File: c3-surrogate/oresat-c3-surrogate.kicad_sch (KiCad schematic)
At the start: 62 parts, among them J1 J-SAMTEC-TFM-120-X1-XXX-D-RA, J2 Conn_01x04, J3 Terminal Block, J4 Barrel Jack, J5 Header, J6 Header, Q1 PMV45EN, Q2 DMP3050LVT-7, Q3 PMV45EN, Q4 DMP3050LVT-7, SW1 Slide Switch, SW2 Slide Switch, U1 Trinket-M0, U2 Seeed-USB-to-UART, U3 MAX892LEUA+T

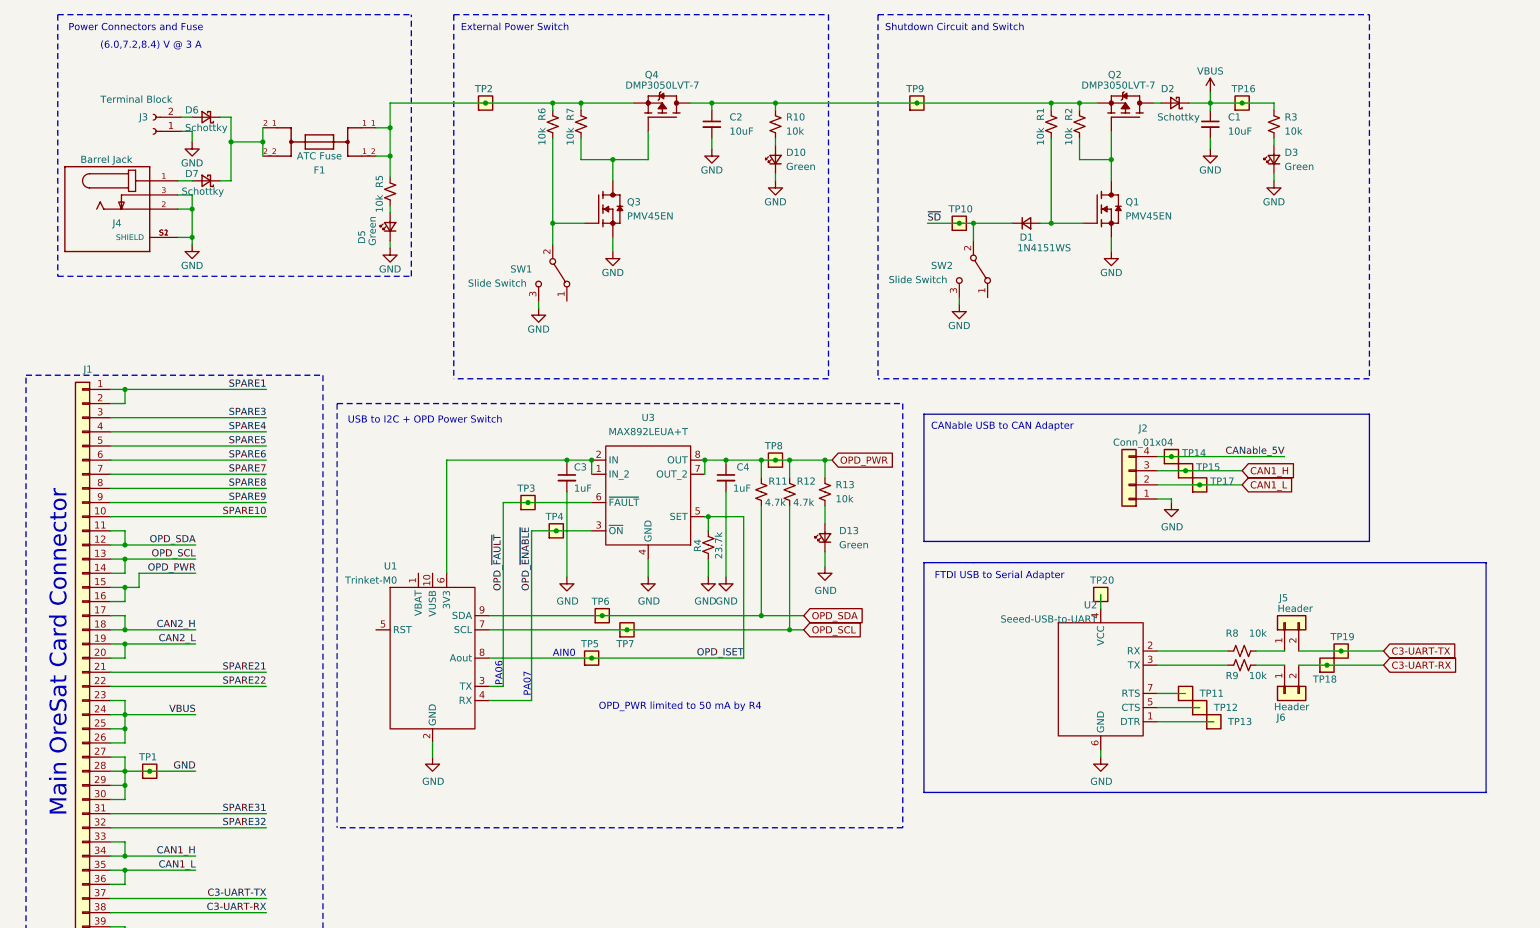
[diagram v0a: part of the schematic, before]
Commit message: updated c3 schematic
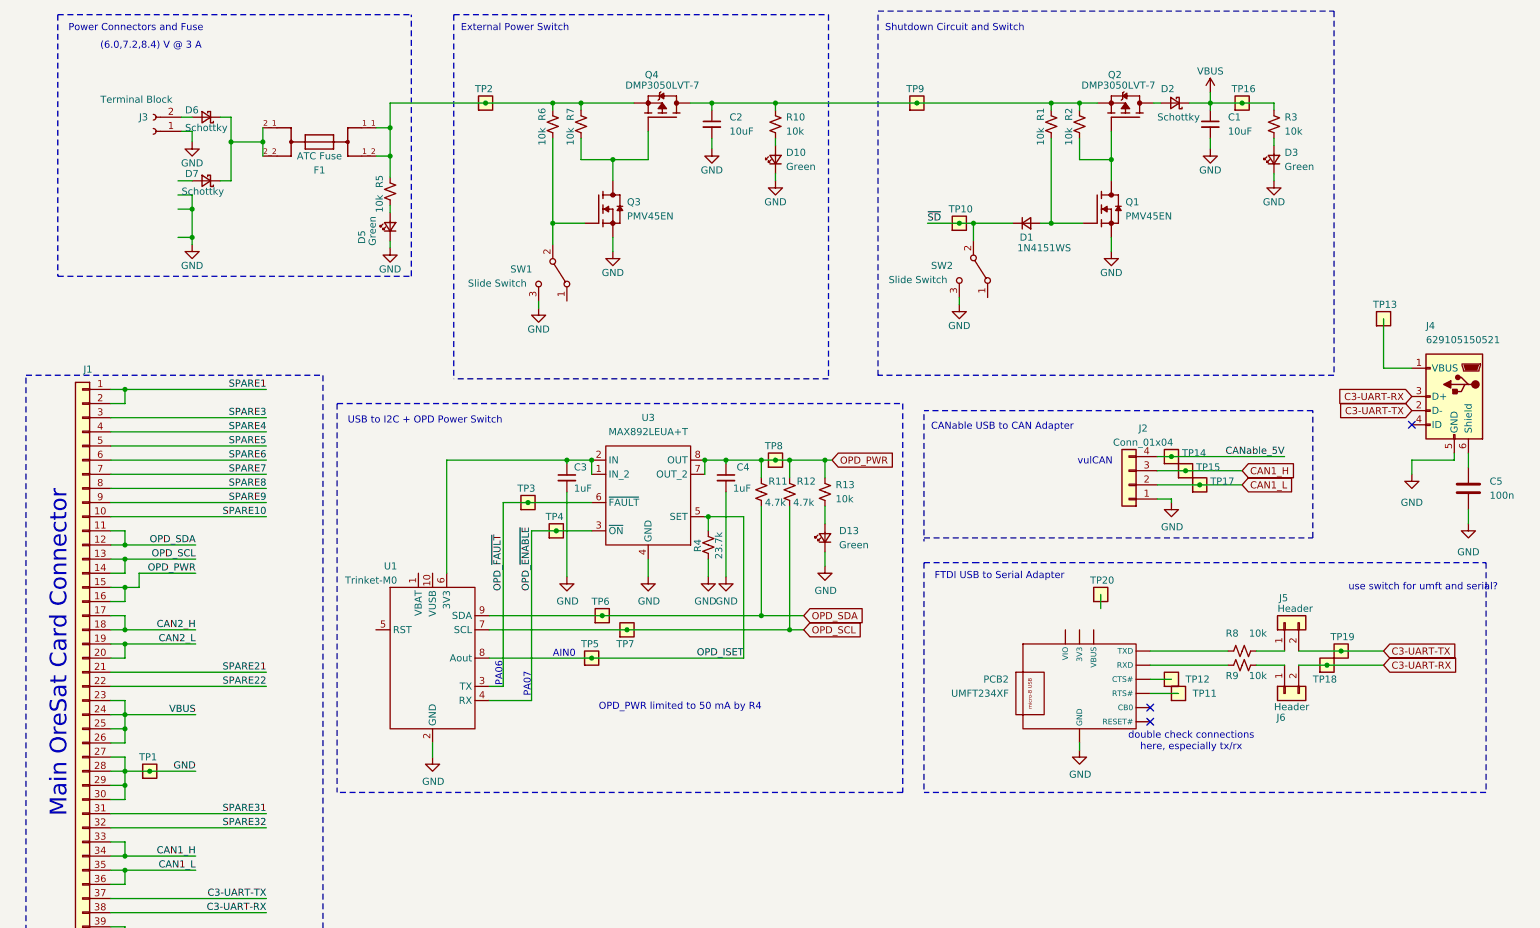
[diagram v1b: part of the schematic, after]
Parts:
- removed J4: Barrel Jack, J-CUI-PJ-051AH-Barrel-Jack:CUI_PJ-051AH, symbol J-CUI-PJ-051AH-Barrel-Jack:PJ-051AH
- removed U2: Seeed-USB-to-UART, Seeed-USB-to-UART:Seeed-USB-to-UART, symbol Seeed-USB-to-UART:Seeed-USB-to-UART
- added C5: 100n, Capacitor_SMD:C_0603_1608Metric, symbol Device:C
- added J4: 629105150521, Connector_USB:USB_Micro-B_Wuerth_629105150521_CircularHoles, symbol Connector:USB_B_Micro
- added PCB2: UMFT234XF, oresat-misc:UMFT234XF, symbol oresat-pcbs:UMFT234XF
- J2: footprint TerminalBlock_4Ucon:TerminalBlock_4Ucon_1x04_P3.50mm_Vertical -> Connector_PinHeader_2.54mm:PinHeader_1x04_P2.54mm_Vertical
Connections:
- net C3-UART-RX: now also J4.3 (D+)
- net C3-UART-TX: now also J4.2 (D-)
- net GND: now also C5.2, J4.5 (GND), PCB2.P4 (GND)
- net at TP13.1: now also J4.1 (VBUS)
- net at TP11.1: now also PCB2.P8 (RTS#)
- net at TP12.1: now also PCB2.P10 (CTS#)
- net at R9.1: now also PCB2.P9 (RXD)
- net at R8.1: now also PCB2.P7 (TXD)
- new net: C5.1, J4.6 (Shield)
- no-connect marks 0 -> 3
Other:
- note added: "double check connections here, especially tx/rx"
- note added: "use switch for umft and serial?"
- note added: "vulCAN"
- moved on the sheet: TP11, TP12

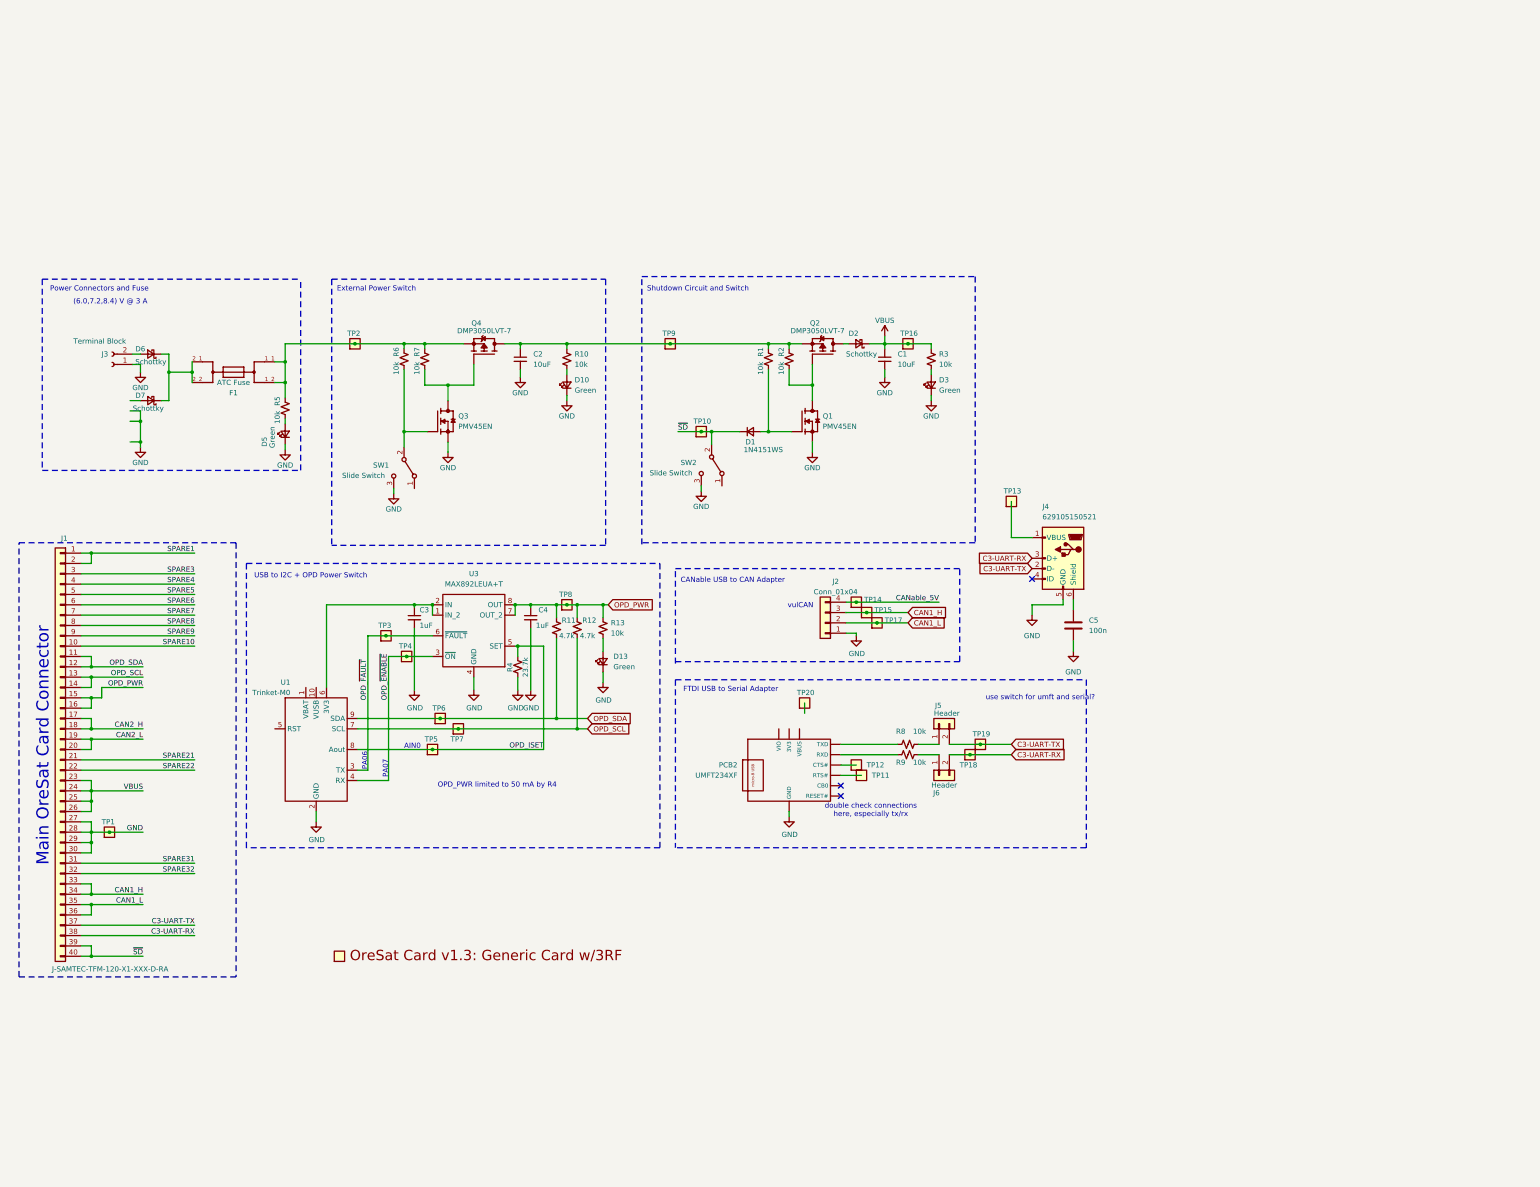
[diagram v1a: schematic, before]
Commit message: added switches and LTC4412 to schematic
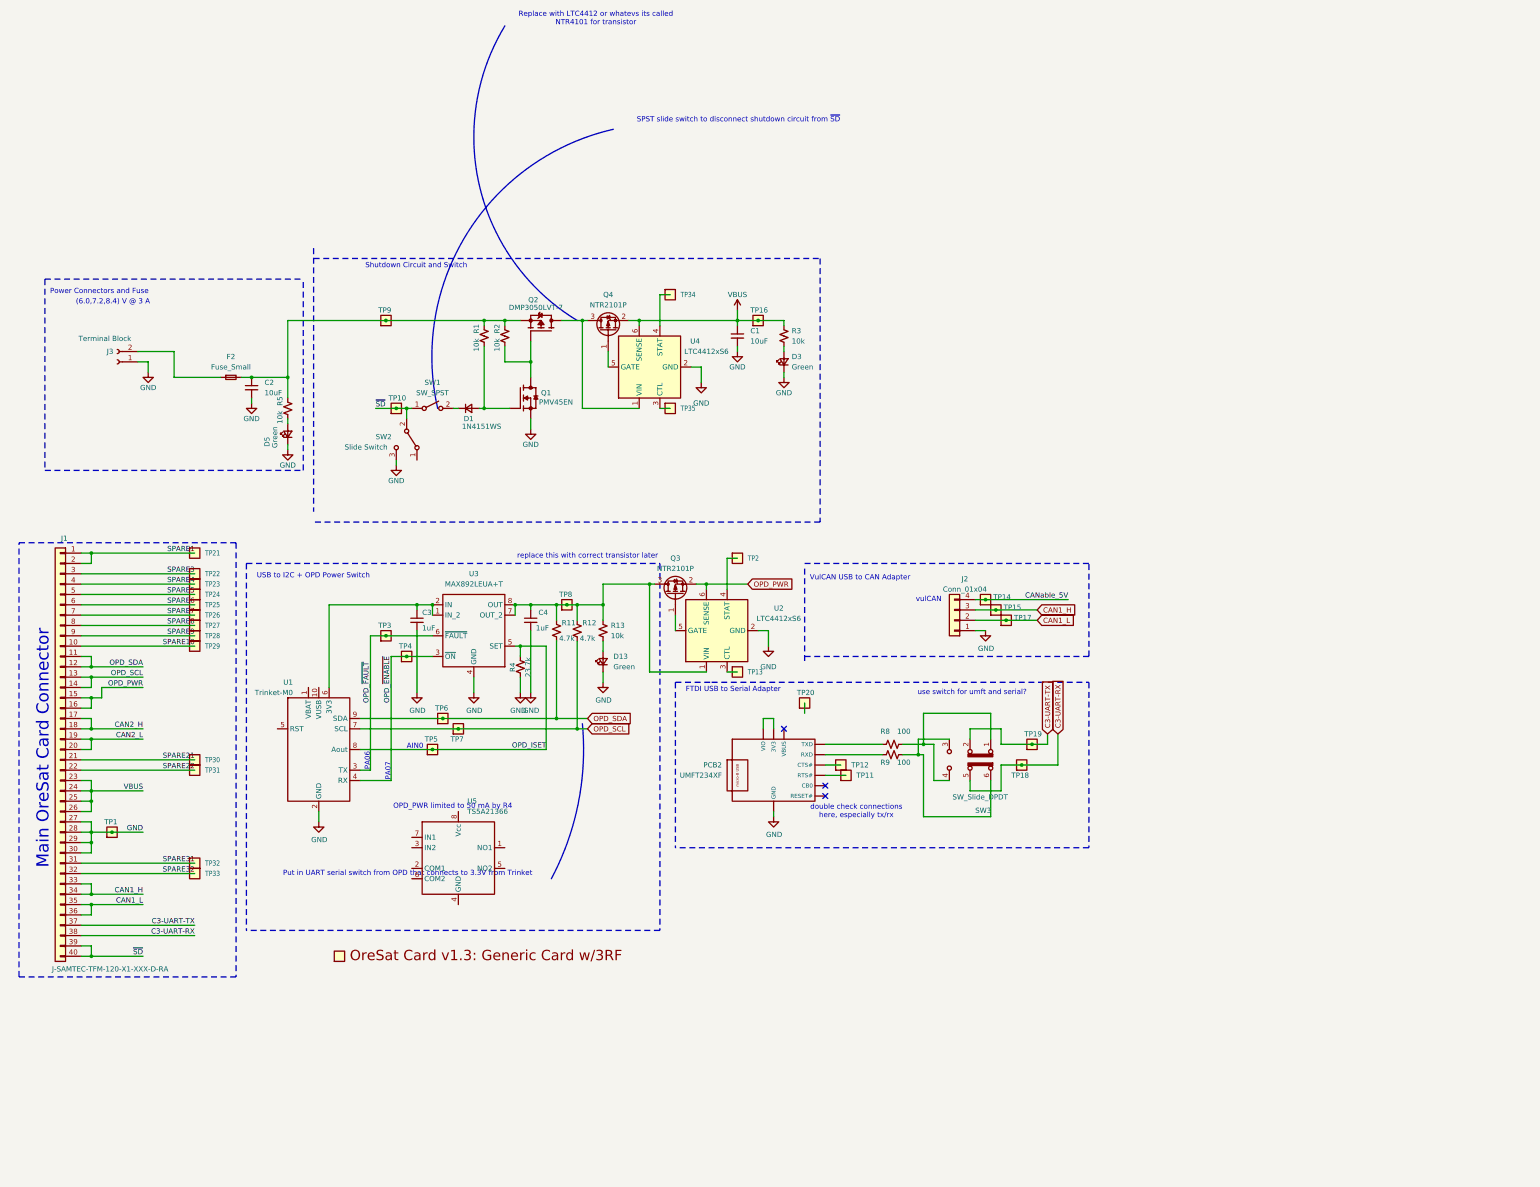
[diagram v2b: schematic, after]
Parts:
- removed C5: 100n, Capacitor_SMD:C_0603_1608Metric, symbol Device:C
- removed D10: Green, LED_SMD:LED_0603_1608Metric_Pad1.05x0.95mm_HandSolder, symbol Device:LED_Small
- removed D2, D6, D7: Schottky, Diode_SMD:D_SMA, symbol Device:D_Schottky_Small
- removed F1: ATC Fuse, F-Keystone-3550-2-ATC-Fuse-Holder:FUSE_3550-2, symbol F-Keystone-3550-2-ATC-Fuse-Holder:3550-2
- removed J4: 629105150521, Connector_USB:USB_Micro-B_Wuerth_629105150521_CircularHoles, symbol Connector:USB_B_Micro
- removed J5, J6: Header, Connector_PinHeader_2.54mm:PinHeader_1x02_P2.54mm_Horizontal, symbol Connector_Generic:Conn_01x02
- removed Q3: PMV45EN, Mosfets:SOT23-3, symbol MOSFET:N-MOSFET-SOT-23-3
- removed Q4: DMP3050LVT-7, Mosfets:SOT23-6, symbol MOSFET:MOSFET-PCH-SOT23-6
- removed R10, R6, R7: 10k, Resistor_SMD:R_0603_1608Metric_Pad0.98x0.95mm_HandSolder, symbol Device:R_Small_US
- removed SW1: Slide Switch, S-CK-AYZ0102AGRLC-Slide-Switch:AYZ0102AGRLC, symbol Switch:SW_SPDT
- removed TP13, TP2: TEST-POINT-LARGE-SQUARE, oresat-misc:1X01, symbol oresat-misc:TEST-POINT-LARGE-SQUARE
- added F2: Fuse_Small, oresat-passives:Littelfuse 155900DR, symbol Device:Fuse_Small
- added Q3, Q4: NTR2101P, Package_TO_SOT_SMD:SOT-23, symbol Transistor_FET:NTR2101P
- added SW1: SW_SPST, symbol Switch:SW_SPST
- added SW3: SW_Slide_DPDT, symbol Switch:SW_Slide_DPDT
- added TP13, TP2, TP21, TP22, TP23, TP24, TP25, TP26, TP27, TP28, TP29, TP30, TP31, TP32, TP33, TP34, TP35: Test-Point, oresat-misc:TestPoint-0.75mm-th, symbol oresat-misc:Test-Point-0.75mm-th
- added U2, U4: LTC4412xS6, Package_TO_SOT_SMD:TSOT-23-6, symbol Power_Management:LTC4412xS6
- added U5: TS5A21366, Package_SO:VSSOP-8_2.3x2mm_P0.5mm, symbol oresat-ics:TS5A21366
- R8, R9: value 10k -> 100
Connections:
- net C3-UART-RX: now also SW3.5 (B)
- net C3-UART-TX: now also SW3.2 (B)
- net GND: now also U2.2 (GND), U4.2 (GND)
- net OPD_PWR: now also Q3.2 (S), U2.6 (SENSE); no longer C4.1, R11.1, R12.1, R13.1, TP8.1, U3.7 (OUT_2), U3.8 (OUT)
- net SPARE1: now also TP21.1
- net SPARE10: now also TP29.1
- net SPARE21: now also TP30.1
- net SPARE22: now also TP31.1
- net SPARE3: now also TP22.1
- net SPARE31: now also TP32.1
- net SPARE32: now also TP33.1
- net SPARE4: now also TP23.1
- net SPARE5: now also TP24.1
- net SPARE6: now also TP25.1
- net SPARE7: now also TP26.1
- net SPARE8: now also TP27.1
- net SPARE9: now also TP28.1
- net VBUS: now also Q4.2 (S), U4.6 (SENSE)
- net ~{SD}: now also SW1.1 (A); no longer D1.1 (K)
- net at C2.1, Q2.4, R1.1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: now also R5.1, F2.2
- net at R9.2: now also SW3.3 (C), SW3.6 (C)
- net at PCB2.P2 (3V3): now also PCB2.P3 (VIO)
- net at Q2.1, Q2.2, Q2.5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: now also Q4.3 (D), U4.1 (VIN)
- net at R8.2: now also SW3.1 (A), SW3.4 (A)
- net at J3.2 (Pin_2): now also F2.1
- new net: D1.1 (K), SW1.2 (B)
- new net: C4.1, Q3.3 (D), R11.1, R12.1, R13.1, TP8.1, U2.1 (VIN), U3.7 (OUT_2), U3.8 (OUT)
- new net: Q4.1 (G), U4.5 (GATE)
- new net: TP13.1, U2.3 (CTL)
- new net: TP2.1, U2.4 (STAT)
- new net: Q3.1 (G), U2.5 (GATE)
- new net: TP35.1, U4.3 (CTL)
- new net: TP34.1, U4.4 (STAT)
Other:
- note added: "Put in UART serial switch from OPD that connects to 3.3V from Trinket"
- note added: "Replace with LTC4412 or whatevs its called NTR4101 for transistor"
- note added: "SPST slide switch to disconnect shutdown circuit from ~{SD}"
- note added: "VulCAN USB to CAN Adapter"
- note added: "replace this with correct transistor later"
- note removed: "CANable USB to CAN Adapter"
- note removed: "External Power Switch"
- moved on the sheet: C1, C2, C3, C4, D1, D3, D5, J2, J3, PCB2, Q1, Q2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

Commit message: finished schematic, updated pcb
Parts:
- removed J3: Terminal Block, J-Phoenix-2-Position-3-5mm-Terminal-Block-Header:1995499, symbol Connector:Conn_01x02_Female
- removed Q2: DMP3050LVT-7, Mosfets:SOT23-6, symbol MOSFET:MOSFET-PCH-SOT23-6
- removed SW1: SW_SPST, symbol Switch:SW_SPST
- removed SW3: SW_Slide_DPDT, symbol Switch:SW_Slide_DPDT
- removed TP1, TP10, TP11, TP12, TP14, TP15, TP16, TP17, TP18, TP19, TP20, TP3, TP4, TP5, TP6, TP7, TP8, TP9: TEST-POINT-LARGE-SQUARE, oresat-misc:1X01, symbol oresat-misc:TEST-POINT-LARGE-SQUARE
- removed U1: Trinket-M0, Adafruit-Trinket-M0:Trinket-M0, symbol Adafruit-Trinket-M0:Trinket-M0
- removed U3: MAX892LEUA+T, U-Maxim-MAX892LEUA+T-power-switch:MAX892LEUA+T, symbol U-Maxim-MAX892LEUA+T-power-switch:MAX892LEUA+T
- added J4: Conn_01x02_Socket, oresat-connectors:PHOENIX_1995499, symbol Connector:Conn_01x02_Socket
- added Q5: DMP3050LVT-7, Package_TO_SOT_SMD:SOT-23-6, symbol oresat-transistors:DMP3050LVT-7
- added SW3: OS203011MV9QS1, DP3T_OS203011MV9QS1_CNK, symbol oresat-passives:OS203011MV9QS1
- added SW4: EG1218, Connector_PinHeader_2.54mm:PinHeader_1x03_P2.54mm_Vertical, symbol Switch:SW_SPDT_321
- added TP1, TP10, TP11, TP12, TP14, TP15, TP16, TP17, TP18, TP19, TP3, TP4, TP5, TP6, TP7, TP8, TP9: Test-Point, oresat-misc:TestPoint-0.75mm-th, symbol oresat-misc:Test-Point-0.75mm-th
- added U1: MAX892LEUA+T, oresat-passives:MAX892, symbol oresat-passives:MAX892LEUA+T
- added U6: Trinket-M0, oresat-mcu:Adafruit-Trinket, symbol oresat-pcbs:Trinket-M0
- Q1: symbol MOSFET:N-MOSFET-SOT-23-3 -> Device:Q_NMOS_GSD
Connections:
- net C3-UART-RX: now also SW3.4, SW3.9, TP19.1
- net C3-UART-TX: now also SW3.2, SW3.7, TP18.1
- net CAN1_H: now also TP15.1
- net CAN1_L: now also TP17.1
- net CANable_5V: now also TP14.1
- net GND: now also U5.4 (GND), J4.1 (Pin_1), TP1.1, U1.4 (GND), U6.2 (GND)
- net OPD_ISET: now also TP5.1, U1.5 (SET), U6.8 (Aout)
- net OPD_SCL: now also U5.5 (NO2); no longer R12.2
- net OPD_SDA: now also U5.1 (NO1); no longer R11.2
- net OPD_~{ENABLE}: now also TP3.1, U1.3 (~{ON}), U6.4 (RX)
- net OPD_~{FAULT}: now also TP4.1, U1.6 (~{FAULT}), U6.3 (TX)
- net VBUS: now also TP16.1
- net ~{SD}: now also SW4.1 (C), TP10.1
- net at D1.1 (K): now also SW4.2 (B)
- net at C3.1: now also U5.3 (IN2), U5.7 (IN1), U5.8 (Vcc), U1.1 (IN_2), U1.2 (IN), U6.6 (3V3)
- net at C4.1, Q3.3 (D), R11.1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: now also TP8.1, U1.7 (OUT_2), U1.8 (OUT)
- net at PCB2.P8 (RTS#): now also TP12.1
- net at Q4.3 (D), U4.1 (VIN): now also Q5.1 (D), Q5.2 (D), Q5.5 (D), Q5.6 (D)
- net at PCB2.P10 (CTS#): now also TP11.1
- net at U5.2 (COM1): now also R11.2
- net at U5.6 (COM2): now also R12.2
- net at C2.1, F2.2, R1.1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: now also Q5.4 (S), TP9.1
- net at F2.1: now also J4.2 (Pin_2)
- net at R9.2: now also SW3.1
- net at R8.2: now also SW3.10
- net at Q1.3 (D), R2.2: now also Q5.3 (G)
- new net: TP6.1, U6.7 (SCL)
- new net: TP7.1, U6.9 (SDA)
- no-connect marks 3 -> 12
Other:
- note removed: "Put in UART serial switch from OPD that connects to 3.3V from Trinket"
- note removed: "Replace with LTC4412 or whatevs its called NTR4101 for transistor"
- note removed: "SPST slide switch to disconnect shutdown circuit from ~{SD}"
- note removed: "double check connections here, especially tx/rx"
- note removed: "use switch for umft and serial?"
- moved on the sheet: C3, D1
